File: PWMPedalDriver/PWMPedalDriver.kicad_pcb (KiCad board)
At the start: 2 copper layers, 0 parts

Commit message: First pass placement
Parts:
- added C1: 400n, Capacitor_SMD:C_0402_1005Metric_Pad0.74x0.62mm_HandSolder, B.Cu at (156.2, 88.1)
- added H1: MountingHole, MountingHole:MountingHole_3.2mm_M3, F.Cu at (144.8, 71.1)
- added H2: MountingHole, MountingHole:MountingHole_3.2mm_M3, F.Cu at (144.8, 99.1)
- added H3: MountingHole, MountingHole:MountingHole_3.2mm_M3, F.Cu at (172.7, 99.1)
- added H4: MountingHole, MountingHole:MountingHole_3.2mm_M3, F.Cu at (172.7, 71.1)
- added J1: Conn_01x01_Pin, Connector_PinHeader_2.54mm:PinHeader_1x01_P2.54mm_Vertical, F.Cu at (167.6, 83.8)
- added J2: Conn_01x01_Pin, Connector_PinHeader_2.54mm:PinHeader_1x01_P2.54mm_Vertical, F.Cu at (157.5, 96.5)
- added J3: Conn_01x02_Pin, Connector_PinHeader_2.54mm:PinHeader_1x02_P2.54mm_Vertical, F.Cu at (149.4, 83.8)
- added R10: 50k, Resistor_SMD:R_0402_1005Metric_Pad0.72x0.64mm_HandSolder, F.Cu at (149.9, 79.5)
- added R11: 50k, Resistor_SMD:R_0402_1005Metric_Pad0.72x0.64mm_HandSolder, F.Cu at (152.0, 78.7)
- added R12: R, Resistor_SMD:R_0402_1005Metric_Pad0.72x0.64mm_HandSolder, B.Cu at (157.5, 88.1)
- added R13: 10k, Resistor_SMD:R_0402_1005Metric_Pad0.72x0.64mm_HandSolder, B.Cu at (152.6, 82.5)
- added R2: 10k, Resistor_SMD:R_0402_1005Metric_Pad0.72x0.64mm_HandSolder, B.Cu at (151.9, 84.5)
- added R3: 4k, Resistor_SMD:R_0402_1005Metric_Pad0.72x0.64mm_HandSolder, B.Cu at (157.0, 82.0)
- added R4: 0, Resistor_SMD:R_0402_1005Metric_Pad0.72x0.64mm_HandSolder, B.Cu at (159.5, 88.1)
- added R5: 0, Resistor_SMD:R_0402_1005Metric_Pad0.72x0.64mm_HandSolder, F.Cu at (163.3, 83.1)
- added R6: 0, Resistor_SMD:R_0402_1005Metric_Pad0.72x0.64mm_HandSolder, B.Cu at (158.2, 94.1)
- added R7: 0, Resistor_SMD:R_0402_1005Metric_Pad0.72x0.64mm_HandSolder, B.Cu at (156.7, 94.1)
- added R8: 100k, Resistor_SMD:R_0402_1005Metric_Pad0.72x0.64mm_HandSolder, F.Cu at (165.6, 80.4)
- added R9: 0, Resistor_SMD:R_0402_1005Metric_Pad0.72x0.64mm_HandSolder, F.Cu at (167.6, 88.5)
- added TP2: TestPoint, TestPoint:TestPoint_Loop_D2.60mm_Drill0.9mm_Beaded, F.Cu at (163.8, 86.4)
- added TP3: TestPoint, TestPoint:TestPoint_Loop_D2.60mm_Drill0.9mm_Beaded, F.Cu at (163.8, 90.4)
- added TP4: TestPoint, TestPoint:TestPoint_Loop_D2.60mm_Drill0.9mm_Beaded, F.Cu at (155.2, 78.0)
- added U1: LM324, Package_SO:SOIC-14_3.9x8.7mm_P1.27mm, F.Cu at (157.5, 85.1)
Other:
- board outline added: 35.3 x 35.1 mm

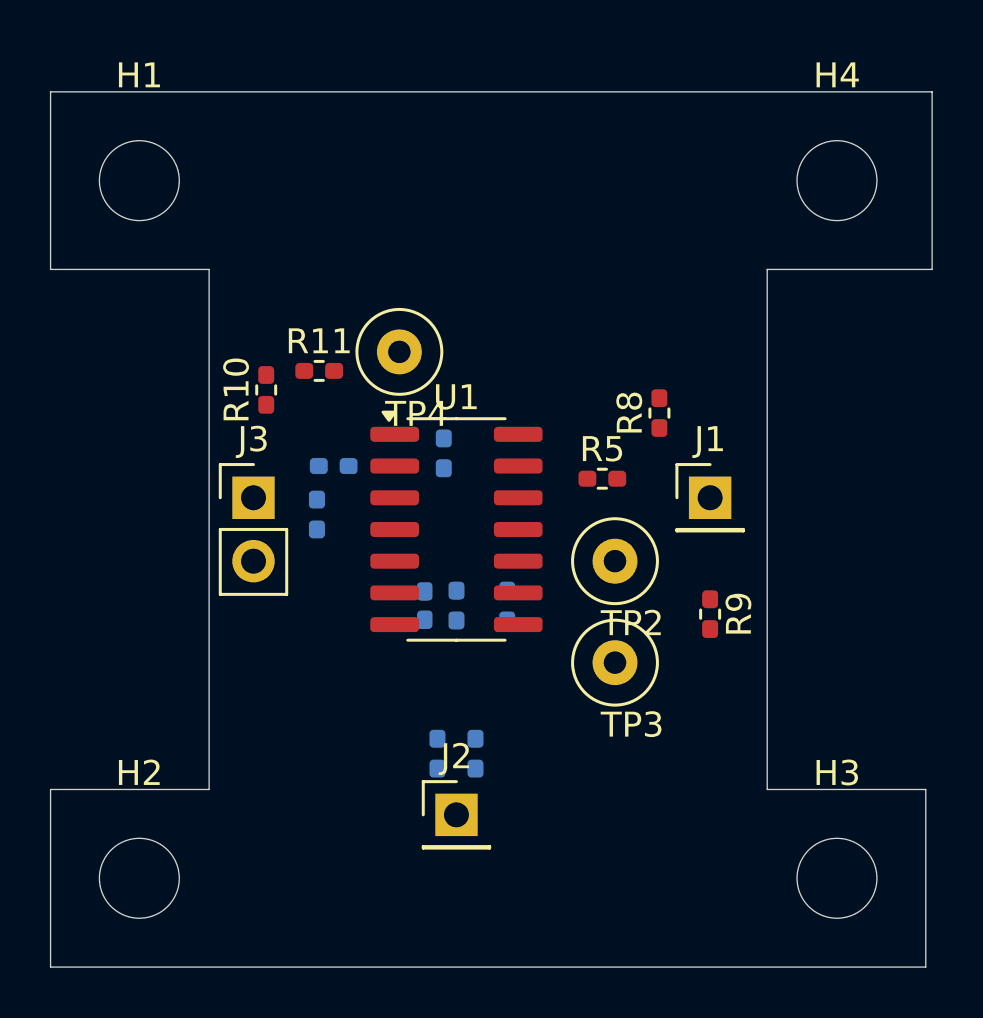
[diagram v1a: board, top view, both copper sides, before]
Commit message: Potential Routing / Placement for PWM
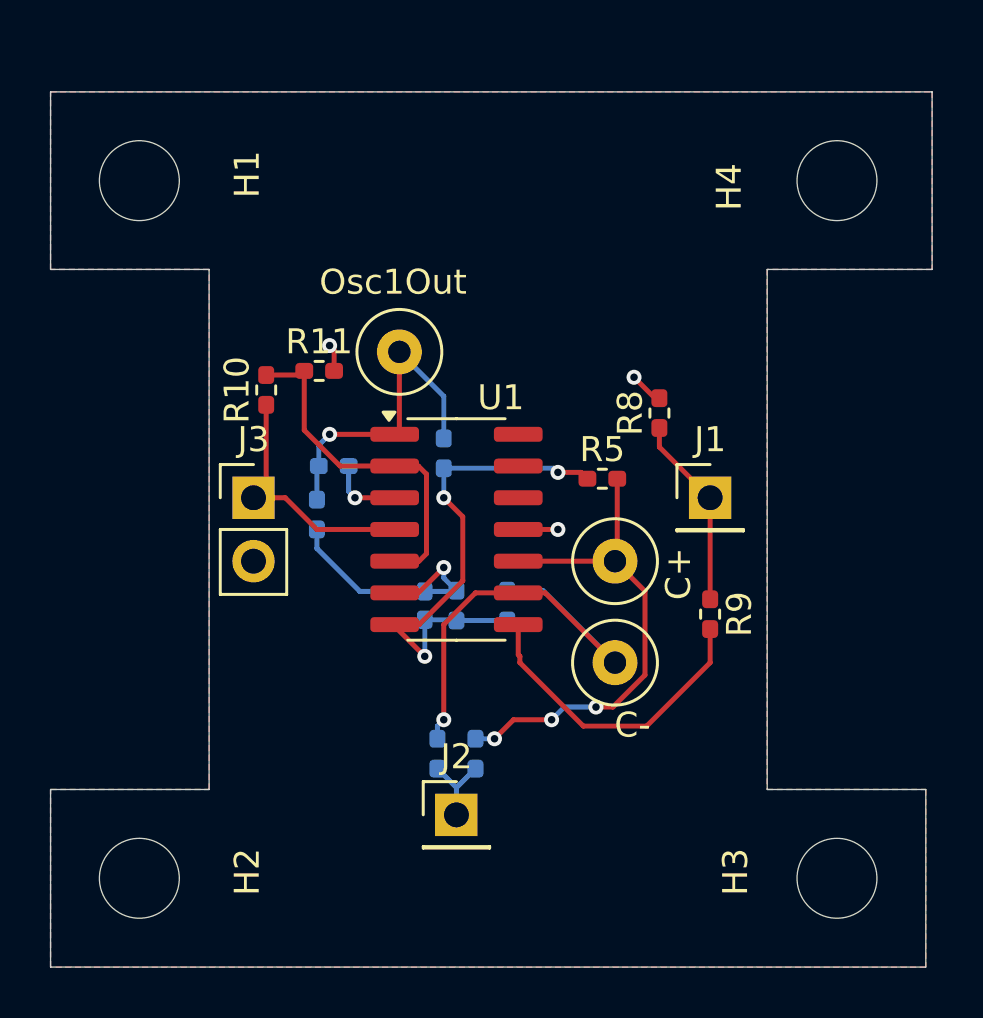
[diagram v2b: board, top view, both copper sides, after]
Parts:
- R12: value R -> 100k_NP
- renumbered TP2 to C+, TP3 to C-, TP4 to Osc1Out
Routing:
- net Net-(C1-Pad2): track 0.00 -> 20.8 mm, vias 0 -> 3
- net Net-(U1C-+): track 0.00 -> 20.1 mm, vias 0 -> 3
- net Net-(U1C--): track 0.00 -> 18.7 mm, vias 0 -> 1
- net /Ref: track 0.00 -> 14.2 mm
- net Net-(Osc1Out1-Pad1): track 0.00 -> 13.0 mm, vias 0 -> 1
- net Net-(R9-Pad2): track 0.00 -> 12.6 mm
- net Net-(U1B--): track 0.00 -> 10.6 mm, vias 0 -> 1
- net /VCC: track 0.00 -> 10.1 mm
- net Net-(J1-Pin_1): track 0.00 -> 7.70 mm
- net GND: track 0.00 -> 4.04 mm, vias 0 -> 3
- net /AnalogIn: track 0.00 -> 3.25 mm
- net Net-(U1A-+): track 0.00 -> 2.96 mm, vias 0 -> 1
- added copper zone on B.Cu, net GND
- added copper zone on F.Cu, net GND

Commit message: Shipped Board
Shipped out the Analog -> PWM driver
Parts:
- removed H1, H2: MountingHole, MountingHole:MountingHole_3.2mm_M3
- moved H3 7.11 mm to (172.7, 91.9)
- moved H4 7.11 mm to (172.7, 78.2)
- moved J2 4.17 mm to (154.2, 94.0)
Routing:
- net /AnalogIn: track 3.25 -> 4.35 mm
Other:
- board size 35.3 x 35.1 mm -> 28.7 x 20.8 mm
